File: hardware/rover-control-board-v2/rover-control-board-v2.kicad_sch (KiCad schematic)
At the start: 59 parts, among them J1 XT120, J17 IEC61076-2_M8_A-coding_01x04_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, J2 RET, J3 OUT, J4 CAN1, J5 CAN1, J6 CAN1, J7 XT90_REG_OUT, J8 XT90_REG_RET, J9 Contactor, Q1 MCACD8D5N06YL-TP, Q2 MCACD8D5N06YL-TP, U1 LM74700, U3 NMUX1308BQ, U4 NMUX1308BQ

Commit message: revamping channel switches
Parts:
- removed BATT_IND1: LTST-C190KRKT, LED_SMD:LED_0603_1608Metric, symbol Device:LED
- removed C12, C13, C14, C15, C6, C8: 1nF, symbol Device:C
- removed C5: 50nF, symbol Device:C
- removed C9: 10uF, symbol Device:C_Polarized
- removed Q1, Q2: MCACD8D5N06YL-TP, symbol Transistor_FET:Q_Dual_NMOS_S1G1S2G2D2D2D1D1
- removed R12, R13: 100R, symbol Device:R
- removed U1: LM74700, Package_TO_SOT_SMD:SOT-23-6, symbol Power_Management:LM74700
- removed U3, U4: NMUX1308BQ, Package_DFN_QFN:DHVQFN-16-1EP_2.5x3.5mm_P0.5mm_EP1x2mm, symbol Analog_Switch:NMUX1308BQ
- added Q1: PMOS, symbol Simulation_SPICE:PMOS
- added Q2: CSD19533Q5A, Package_TO_SOT_SMD:TDSON-8-1, symbol Transistor_FET:CSD19533Q5A
- added R11: 10k, symbol Device:R
- added U2: ADS131M08xPBS, Package_QFP:TQFP-32_5x5mm_P0.5mm, symbol Analog_ADC:ADS131M08xPBS
- R10: footprint Resistor_SMD:R_0603_1608Metric -> (none); distributors part number 311-10.0KHRTR-ND -> (none); manufactuer part number RC0603FR-0710KL -> (none); manufacturer YAGEO -> (none)
- R8: value 100R -> 9.53M; digikey_part_num (none) -> 541-9.53MHTR-ND
- R9: value 100R -> 232k; digikey_part_num (none) -> 118-CR0603-FX-2323ELFTR-ND
- U1: renamed from U2; footprint footprints:21-0137I_T633-2_MXM-L -> footprints:max6496
- renumbered C7 to C5, C10 to C6, C11 to C7, J9 to J10, J7 to J3, J3 to J4, J8 to J5, J4 to J6, J5 to J7, J6 to J8, J17 to J9, R11 to R12
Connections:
- net 3V3: now also R10.2, R11.2
- net GND: now also R9.2, U1.5 (GND); no longer R10.2, U1.4 (GND)
- net SCLK: now also R10.1
- net SDATA: now also R11.1
- net VBUS: now also U1.7 (OUTFB), Q2.1 (S), Q2.2 (S), Q2.3 (S); no longer U1.6 (OUTFB)
- net at R8.1: now also U1.1 (IN), U1.2 (_SHDN), Q1.3 (S), Q2.5 (D)
- net at R8.2, R9.1: now also U1.3 (OVSET)
- net at J5.1 (Pin_1), VBUS_TP2.1: now also Q1.1 (D); no longer U1.1 (IN), U1.2 (_SHDN)
- new net: Q1.2 (G), U1.4 (GATEP)
- new net: Q2.4 (G), U1.6 (GATE)
- new net: U2.13 (AGND), U2.27 (AGND), U2.28 (AGND)
- no-connect marks 24 -> 23
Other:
- note removed: "IS EN_ tied good?"
- note removed: "Ideal diode, reverse polarity protection"
- moved on the sheet: J3, J5, VBUS_TP1, VBUS_TP2

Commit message: 10v reg added for charge pumps
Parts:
- added C53: 70nF, symbol Device:C
- added C54, C55, C56: 10uF, Capacitor_SMD:C_0603_1608Metric, symbol Device:C
- added C8: 1nF, symbol Device:C
- added C9: 100nF, symbol Device:C
- added D45: 30v, symbol Device:D_Schottky
- added L2: 22uH, Inductor_SMD:L_Taiyo-Yuden_MD-4040, symbol Device:L
- added R128: 109k, Resistor_SMD:R_0603_1608Metric, symbol Device:R
- added R129: 370k, symbol Device:R
- added R130: 46.6k, symbol Device:R
- added R131: 115k, symbol Device:R
- added R132: 10k, symbol Device:R
- added U3: AOZ1284PI, Package_SO:SOIC-8-1EP_3.9x4.9mm_P1.27mm_EP2.71x3.7mm, symbol Regulator_Switching:AOZ1284PI
- added VIN_IND2: LTST-C190KRKT, LED_SMD:LED_0603_1608Metric, symbol Device:LED
- R1, R2: value 10k -> 223k
- renumbered VBUS_TP1 to VBATT_TP1
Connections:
- net +BATT: now also D4.2 (A2), J1.1 (Pin_1), R6.2, VIN_IND2.2 (A)
- net 3V3: now also U3.8 (EN)
- net GND: now also C53.2, C54.1, C55.2, C56.2, C8.2, D45.2 (A), R128.2, R130.2, R132.1, U3.3 (GND)
- net VBUS: now also C54.2, U3.9 (VIN)
- new net: R128.1, VIN_IND2.1 (K)
- new net: C53.1, R129.2
- new net: C8.1, U3.7 (SS)
- new net: C55.1, C56.1, L2.2, R131.2
- new net: C9.1, U3.2 (BST)
- new net: C9.2, D45.1 (K), L2.1, U3.1 (LX)
- new net: R130.1, U3.4 (FSW)
- new net: R129.1, U3.5 (COMP)
- new net: R131.1, R132.2, U3.6 (FB)
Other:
- note removed: "Could EN to SBB for control"

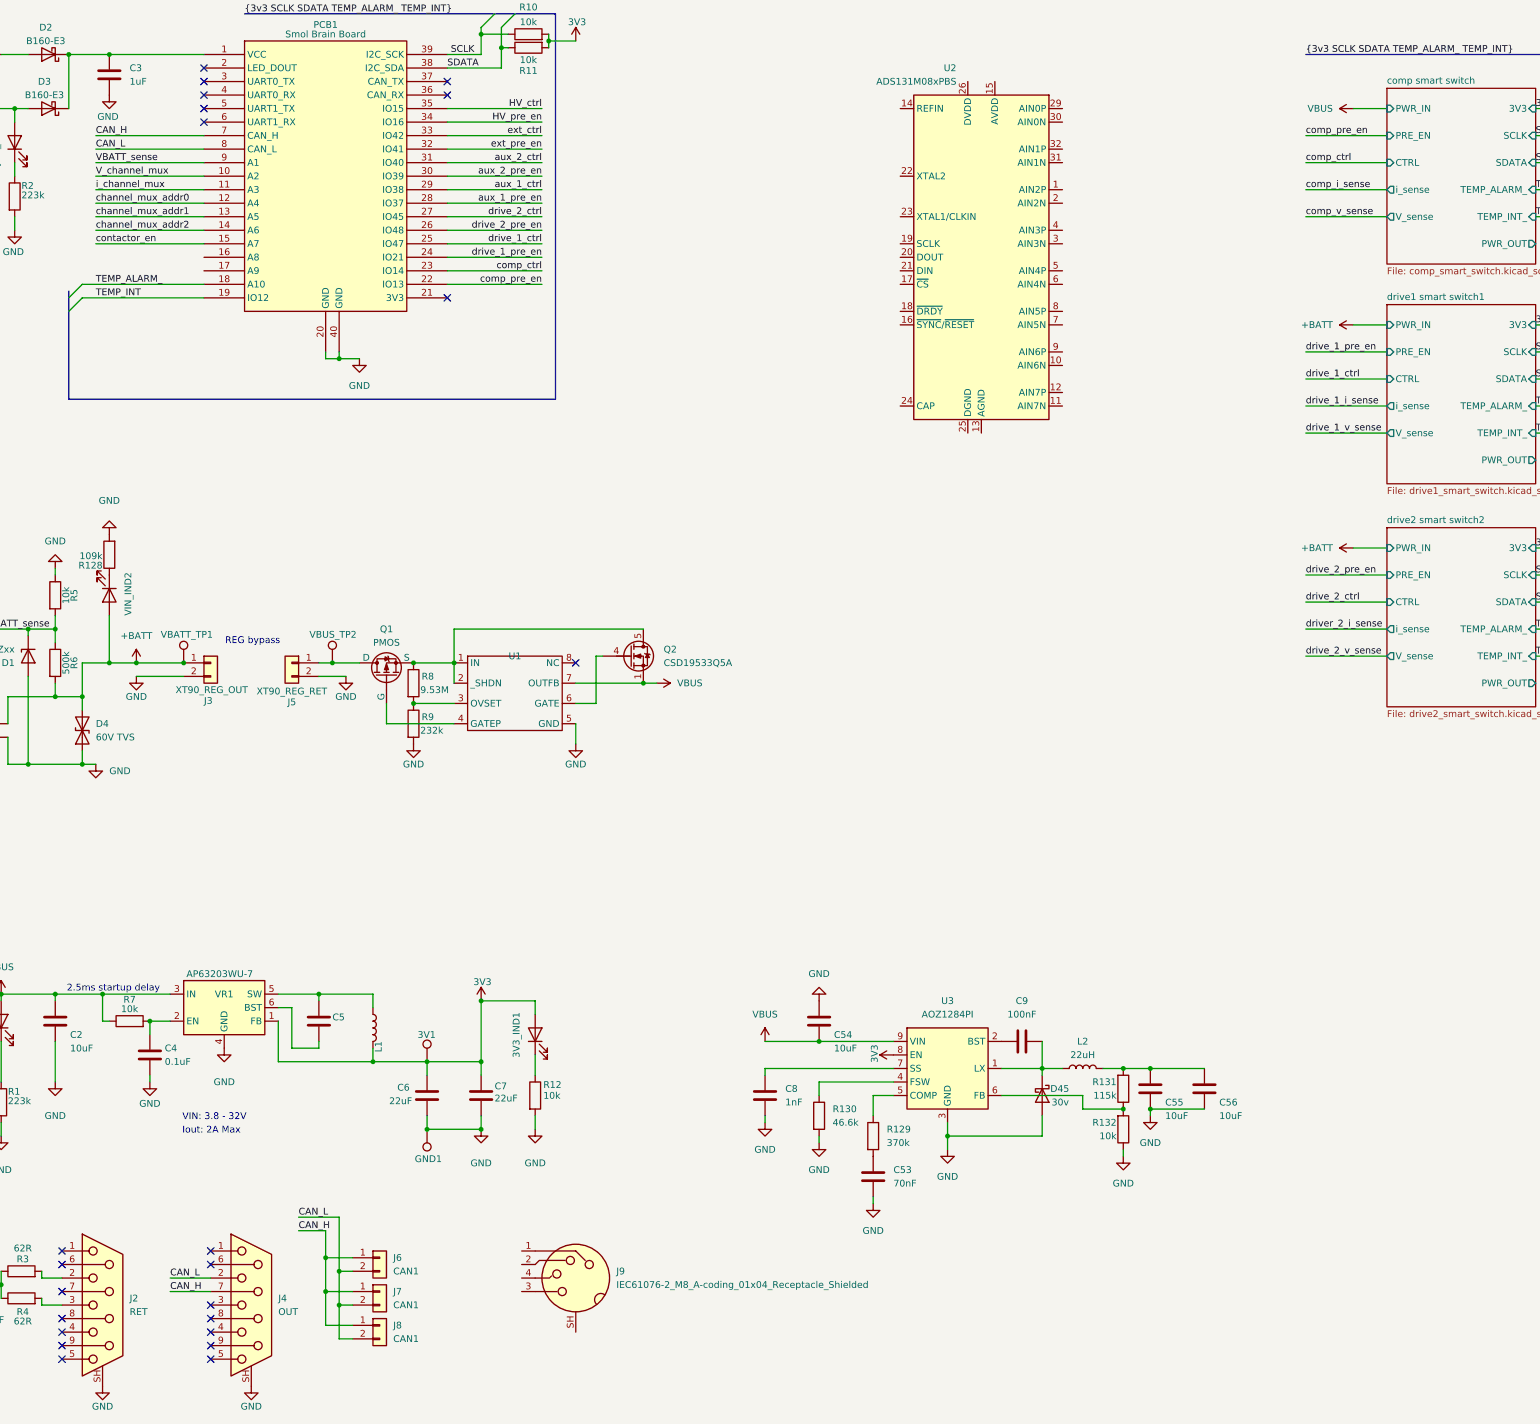
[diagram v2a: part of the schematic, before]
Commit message: high power switch added
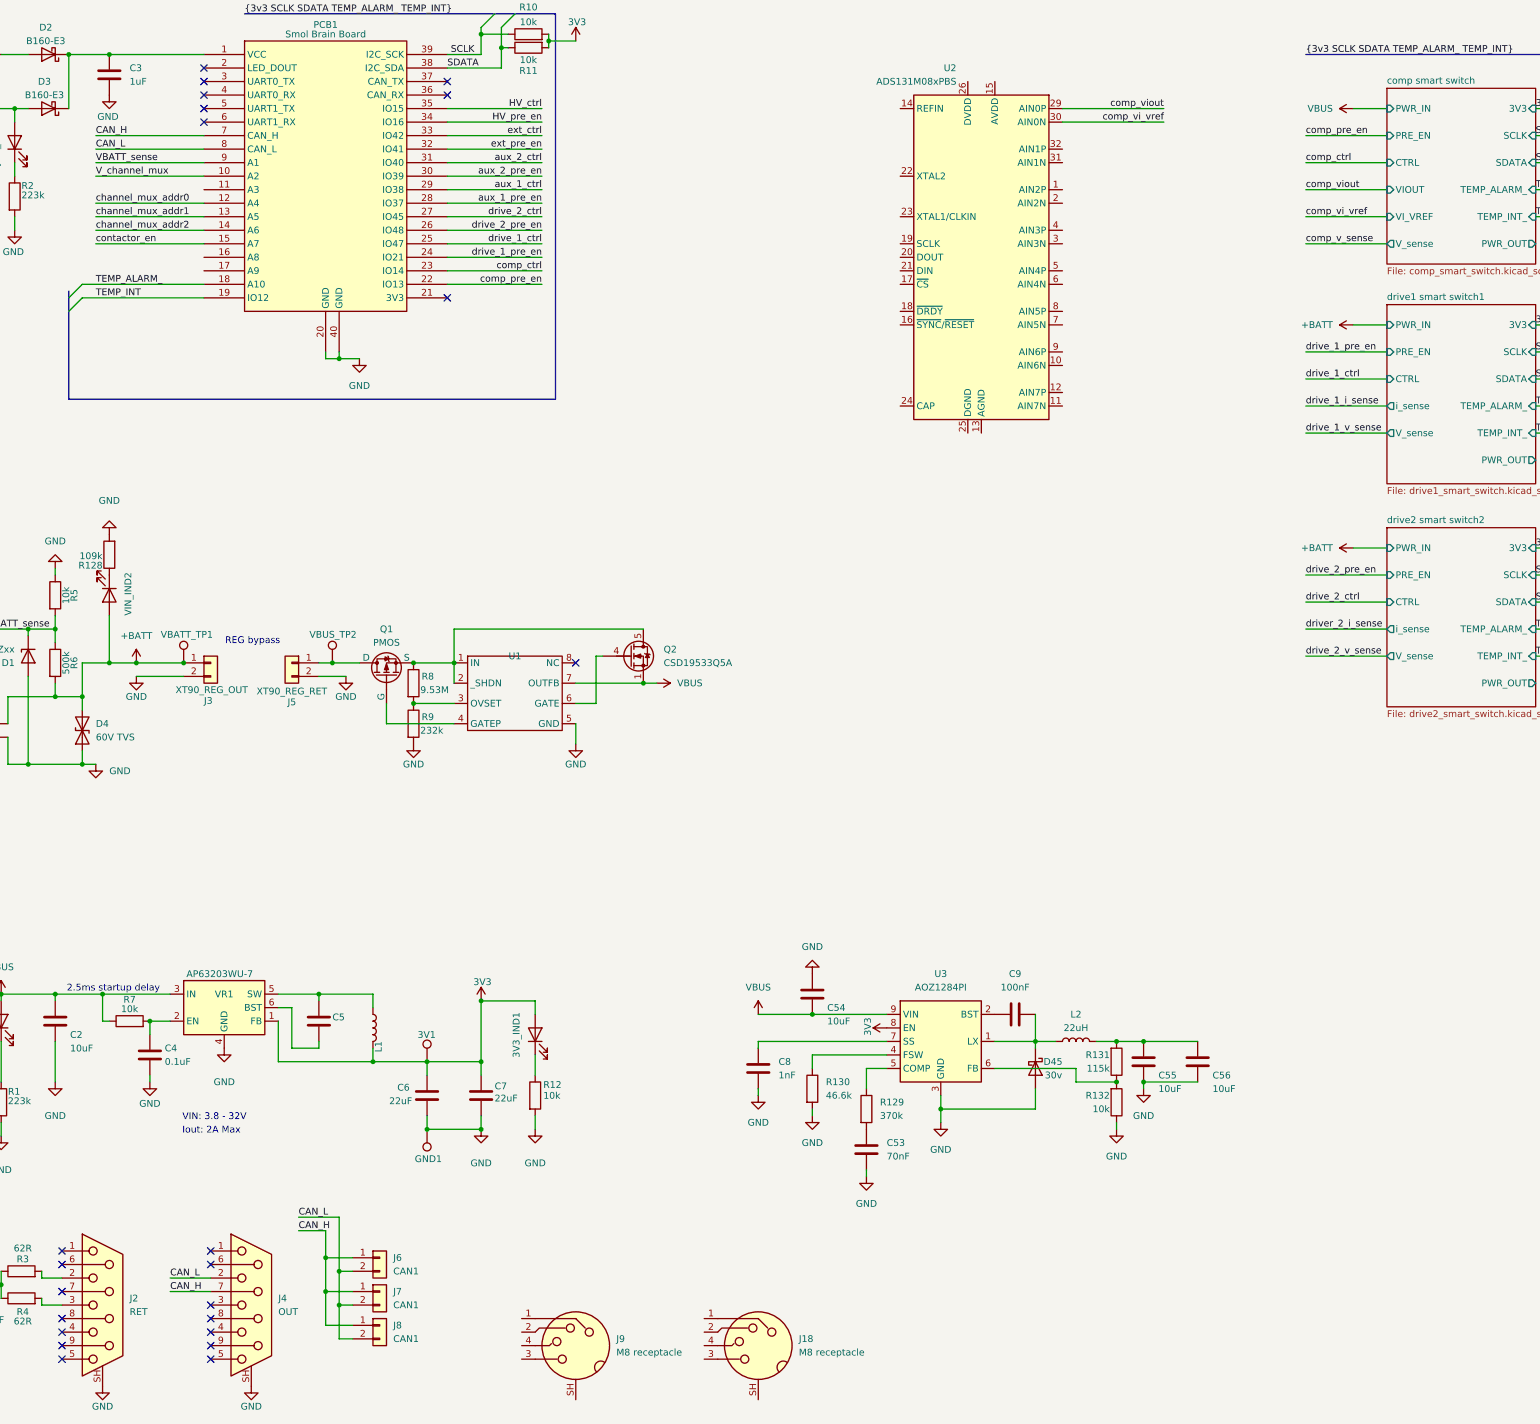
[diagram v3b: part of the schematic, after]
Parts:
- added J18: M8 receptacle, symbol Connector:IEC61076-2_M8_A-coding_01x04_Receptacle_Shielded
- J9: value IEC61076-2_M8_A-coding_01x04_Receptacle_Shielded -> M8 receptacle
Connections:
- net comp_viout: now reaches U2.29 (AIN0P)
- net comp_vi_vref: now reaches U2.30 (AIN0N)
- net i_channel_mux: no longer names the net of PCB1.11 (A3)
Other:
- sheet comp smart switch ports: added VIOUT, VI_VREF; removed i_sense
- moved on the sheet: C53, C54, C55, C56, C8, C9, D45, J9, L2, R129, R130, R131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

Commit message: Minor fixes and sanity checks
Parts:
- added C50: 4.7nF, symbol Device:C
- added R112, R113: 62R, symbol Device:R
- renumbered C53 to C10, C9 to C11, C55 to C12, C56 to C13, C54 to C9, D45 to D5, J18 to J10, J10 to J11, R9 to R10, R10 to R11, R11 to R12, R12 to R13, R130 to R14, R129 to R15, R131 to R16, R132 to R17, R128 to R7, R7 to R8, R8 to R9, U3 to U2, U2 to U3, VBUS_TP2 to VBUS_TP1
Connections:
- net CAN_H: now also J10.2
- net CAN_L: now also J10.1
- net GND: now also J10.SH, J2.3, J4.3, J9.SH, C50.2
- net at R4.2: now also J2.7; no longer J2.3
- net at J9.1: now also R112.2
- net at J9.2: now also R113.2
- net +10V: now reaches C12.1, C13.1, L2.2, R16.2
- new net: C50.1, R112.1, R113.1
- no-connect marks 23 -> 25
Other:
- sheet aux1 smart switch ports: added none; removed TEMP_INT_, i_sense
- sheet aux2 smart switch ports: added none; removed TEMP_INT_, i_sense
- sheet comp smart switch ports: added 10V; removed TEMP_INT_
- sheet drive1 smart switch1 ports: added none; removed TEMP_INT_, i_sense
- note added: "TODO: - Wire up M8 for CAN, decide on daughterboard for CAN. - Add daughterboard XT120 connector - Santity check status lights - Route differential ADC to sensor inputs - Add RS485?? - Add RB558 where appropriate"
- moved on the sheet: J10, J11, J9

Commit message: Bus routing
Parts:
- C1, J2, J4, R3, R4: now not fitted
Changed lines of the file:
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@@
 		(exclude_from_sim no)
 		(in_bom yes)
-		(on_board yes)
+		(on_board no)
 		(in_pos_files yes)
-		(dnp no)
+		(dnp yes)
 		(property "Reference" "#PWR01"
 			(at 20.32 271.78 0)
@@
 		(exclude_from_sim no)
 		(in_bom yes)
-		(on_board yes)
+		(on_board no)
 		(in_pos_files yes)
-		(dnp no)
+		(dnp yes)
 		(property "Reference" "R4"
 			(at 29.464 261.62 90)
@@
 		(exclude_from_sim no)
 		(in_bom yes)
-		(on_board yes)
+		(on_board no)
 		(in_pos_files yes)
-		(dnp no)
+		(dnp yes)
 		(property "Reference" "R3"
 			(at 29.464 251.714 90)
@@
 		(exclude_from_sim no)
 		(in_bom yes)
-		(on_board yes)
+		(on_board no)
 		(in_pos_files yes)
-		(dnp no)
+		(dnp yes)
 		(property "Reference" "#PWR016"
 			(at 72.39 284.48 0)
@@
 		(exclude_from_sim no)
 		(in_bom yes)
-		(on_board yes)
+		(on_board no)
 		(in_pos_files yes)
-		(dnp no)
+		(dnp yes)
 		(property "Reference" "#PWR09"
 			(at 44.45 284.48 0)
@@
 		(exclude_from_sim no)
 		(in_bom yes)
-		(on_board yes)
+		(on_board no)
 		(in_pos_files yes)
-		(dnp no)
+		(dnp yes)
 		(fields_autoplaced yes)
 		(property "Reference" "J2"
@@
 		(exclude_from_sim no)
 		(in_bom yes)
-		(on_board yes)
+		(on_board no)
 		(in_pos_files yes)
-		(dnp no)
+		(dnp yes)
 		(property "Reference" "C1"
 			(at 22.86 261.112 0)
@@
 		(exclude_from_sim no)
 		(in_bom yes)
-		(on_board yes)
+		(on_board no)
 		(in_pos_files yes)
-		(dnp no)
+		(dnp yes)
 		(fields_autoplaced yes)
 		(property "Reference" "J4"
